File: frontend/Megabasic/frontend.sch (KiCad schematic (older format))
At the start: 27 parts, among them CN1 EDGE, CN2 BREAKOUT, P1 CONN_01X02, P2 CONN_01X02, P3 CONN_01X02, P4 CONN_01X02, P5 CONN_01X02, P6 CONN_01X12, Q1 2N7000, T1 4:1, T2 8:1, U1 4050, U2 74LS145

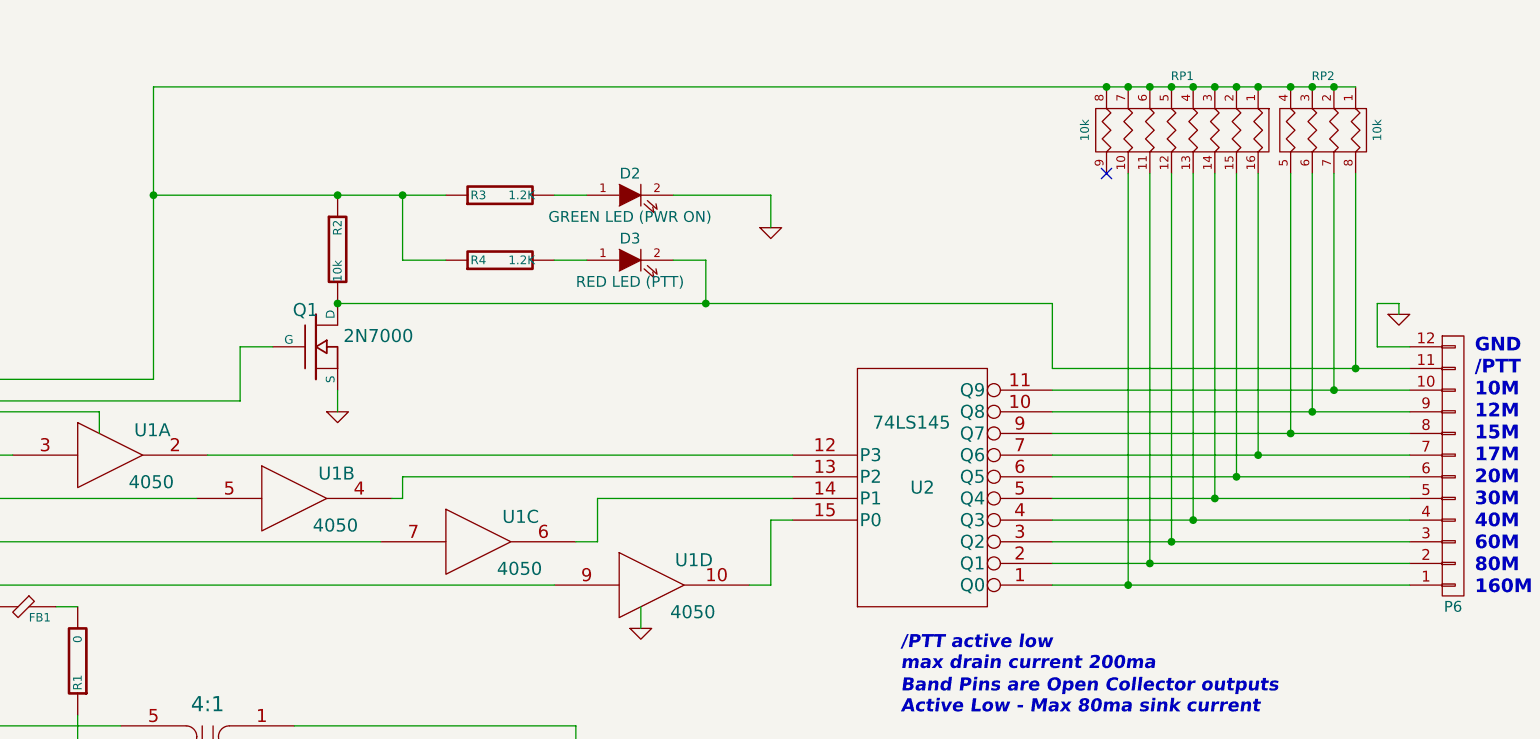
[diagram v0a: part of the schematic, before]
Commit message: modify mounting holes
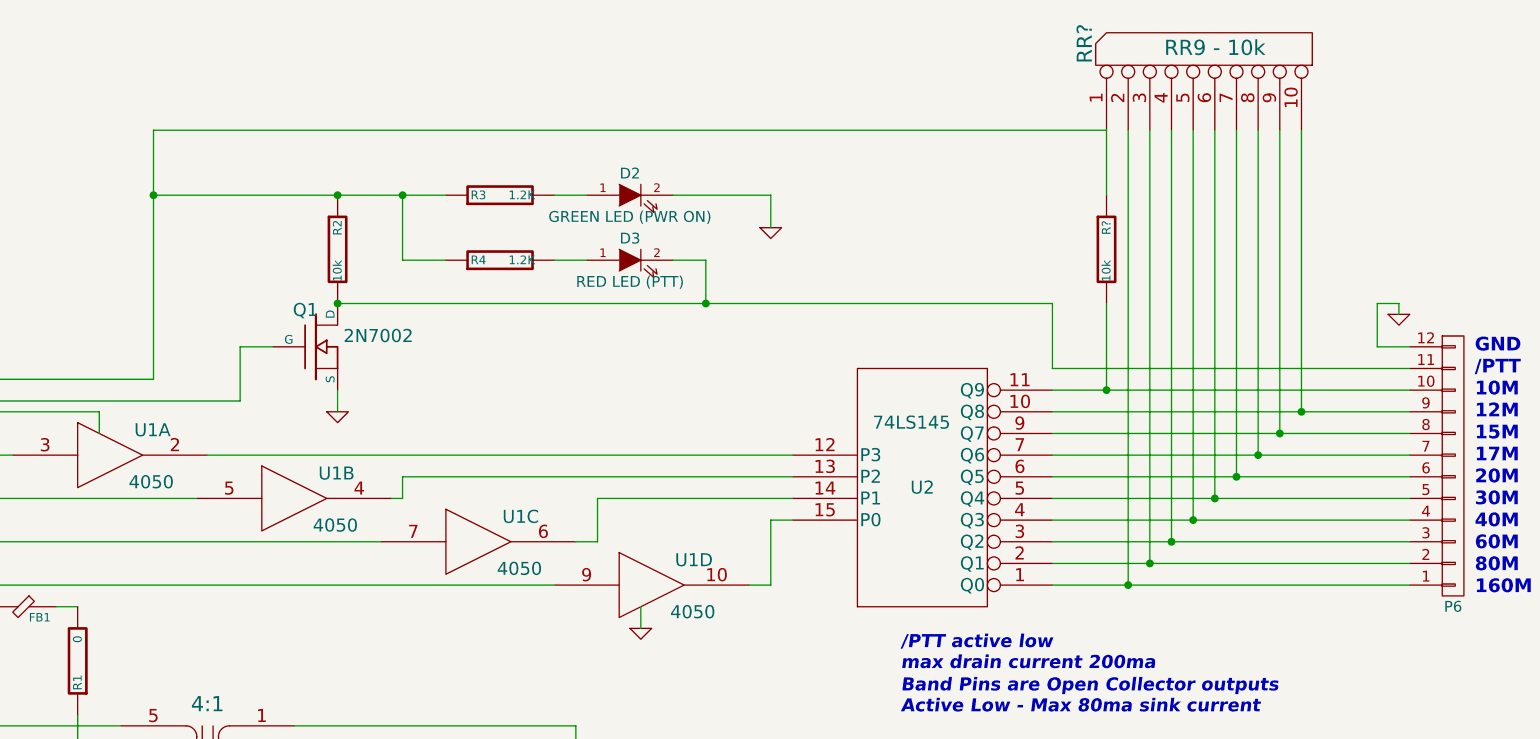
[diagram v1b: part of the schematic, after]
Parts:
- removed RP1: 10k, symbol R_PACK8
- removed RP2: 10k, symbol R_PACK4
- added R?: 10k, symbol R
- added RR?: RR9 - 10k, symbol RR9
- C1, C2, C3, C4, FB1, R1: footprint (none) -> SMD_Packages:SMD-0805
- CN1: footprint (none) -> HERMESLITE:EDGE
- CN2: footprint (none) -> HERMESLITE:BREAKOUT
- D1: footprint (none) -> HERMESLITE:SOD323
- D2, D3: footprint (none) -> LEDs:LED-0805
- P1, P2, P3, P4, P5, P6: footprint (none) -> Pin_Headers:Pin_Header_Straight_1x02
- Q1: value 2N7000 -> 2N7002; footprint (none) -> HERMESLITE:SOT-23-GDS
- R2, R3, R4: footprint (none) -> Resistors_SMD:R_0805_HandSoldering
- T1, T2: footprint (none) -> HERMESLITE:TRANSFREV
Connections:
- net at CN1.A11 (12V), CN1.A12 (12V), CN2.6 (12V)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: now also R?.1, RR?.1 (COM)
- net at P6.1 (P1), U2.1 (Q0): now also RR?.2
- net at P6.10 (P10), U2.11 (Q9): now also R?.2
- net at P6.2 (P2), U2.2 (Q1): now also RR?.3
- net at P6.3 (P3), U2.3 (Q2): now also RR?.4
- net at P6.4 (P4), U2.4 (Q3): now also RR?.5
- net at P6.5 (P5), U2.5 (Q4): now also RR?.6
- net at P6.6 (P6), U2.6 (Q5): now also RR?.7
- net at P6.7 (P7), U2.7 (Q6): now also RR?.8
- net at P6.8 (P8), U2.9 (Q7): now also RR?.9
- net at P6.9 (P9), U2.10 (Q8): now also RR?.10
- no-connect marks 1 -> 0
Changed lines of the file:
@@
 F 0 "CN1" H 1950 3750 60  0000 C CNN
 F 1 "EDGE" H 1950 5800 60  0000 C CNN
-F 2 "" H 1950 4400 60  0000 C CNN
+F 2 "HERMESLITE:EDGE" H 1950 4400 60  0001 C CNN
 F 3 "" H 1950 4400 60  0000 C CNN
 	1    1950 4900
@@
 F 0 "T2" H 4400 5450 70  0000 C CNN
 F 1 "8:1" H 4400 6050 70  0000 C CNN
-F 2 "" H 4400 5750 60  0000 C CNN
+F 2 "HERMESLITE:TRANSFREV" H 4400 5750 60  0001 C CNN
 F 3 "" H 4400 5750 60  0000 C CNN
 	1    4400 5750
@@
 F 0 "T1" H 4400 4000 70  0000 C CNN
 F 1 "4:1" H 4400 4600 70  0000 C CNN
-F 2 "" H 4400 4300 60  0000 C CNN
+F 2 "HERMESLITE:TRANSFREV" H 4400 4300 60  0001 C CNN
 F 3 "" H 4400 4300 60  0000 C CNN
 	1    4400 4300
@@
 F 0 "C3" V 5050 5450 30  0000 L CNN
 F 1 "0.1 uF" V 5050 5600 30  0000 L CNN
-F 2 "" H 5100 5550 60  0000 C CNN
+F 2 "SMD_Packages:SMD-0805" H 5100 5550 60  0001 C CNN
 F 3 "" H 5100 5550 60  0000 C CNN
 	1    5100 5550
@@
 F 0 "C4" V 5450 5450 30  0000 L CNN
 F 1 "0.1 uF" V 5450 5600 30  0000 L CNN
-F 2 "" H 5500 5550 60  0000 C CNN
+F 2 "SMD_Packages:SMD-0805" H 5500 5550 60  0001 C CNN
 F 3 "" H 5500 5550 60  0000 C CNN
 	1    5500 5550
@@
 F 0 "C2" H 3825 6250 30  0000 L CNN
 F 1 "0.1 uF" H 3825 6150 30  0000 L CNN
-F 2 "" H 3800 6200 60  0000 C CNN
+F 2 "SMD_Packages:SMD-0805" H 3800 6200 60  0001 C CNN
 F 3 "" H 3800 6200 60  0000 C CNN
 	1    3800 6200
@@
 F 0 "D1" V 5300 5950 40  0000 C CNN
 F 1 "DIODESCH2" H 5300 5575 40  0001 C CNN
-F 2 "" H 5300 5825 60  0000 C CNN
+F 2 "HERMESLITE:SOD323" H 5300 5825 60  0001 C CNN
 F 3 "" H 5300 5825 60  0000 C CNN
 	1    5300 5750
@@
 F 0 "R1" V 3800 3900 40  0000 C CNN
 F 1 "0" V 3800 3700 40  0000 C CNN
-F 2 "" V 3730 3800 30  0000 C CNN
+F 2 "SMD_Packages:SMD-0805" V 3730 3800 30  0001 C CNN
 F 3 "" H 3800 3800 30  0000 C CNN
 	1    3800 3800
@@
 F 0 "C1" H 3825 4750 30  0000 L CNN
 F 1 "0.1 uF" H 3825 4650 30  0000 L CNN
-F 2 "" H 3800 4700 60  0000 C CNN
+F 2 "SMD_Packages:SMD-0805" H 3800 4700 60  0001 C CNN
 F 3 "" H 3800 4700 60  0000 C CNN
 	1    3800 4700
@@
 F 0 "FB1" H 3625 3500 39  0000 C CNN
 F 1 "FB" H 3550 3650 60  0001 C CNN
-F 2 "" H 3550 3550 60  0000 C CNN
+F 2 "SMD_Packages:SMD-0805" H 3550 3550 60  0001 C CNN
 F 3 "" H 3550 3550 60  0000 C CNN
 	1    3550 3550
@@
 F 0 "CN2" V 2300 800 60  0000 C CNN
 F 1 "BREAKOUT" V 2300 1750 60  0000 C CNN
-F 2 "" H 2250 1300 60  0000 C CNN
+F 2 "HERMESLITE:BREAKOUT" H 2250 1300 60  0001 C CNN
 F 3 "" H 2250 1300 60  0000 C CNN
 	1    2250 1800
@@
 P 4900 2350
 F 0 "Q1" H 4910 2520 60  0000 R CNN
-F 1 "2N7000" H 5350 2400 60  0000 R CNN
-F 2 "" H 4900 2350 60  0000 C CNN
+F 1 "2N7002" H 5350 2400 60  0000 R CNN
+F 2 "HERMESLITE:SOT-23-GDS" H 4900 2350 60  0001 C CNN
 F 3 "" H 4900 2350 60  0000 C CNN
 	1    4900 2350
@@
 F 0 "D2" H 6350 1750 50  0000 C CNN
 F 1 "GREEN LED (PWR ON)" H 6350 1550 50  0000 C CNN
-F 2 "" H 6350 1650 60  0000 C CNN
+F 2 "LEDs:LED-0805" H 6350 1650 60  0001 C CNN
 F 3 "" H 6350 1650 60  0000 C CNN
 	1    6350 1650
@@
 F 0 "R3" V 5750 1750 40  0000 C CNN
 F 1 "1.2K" V 5750 1550 40  0000 C CNN
-F 2 "" V 5680 1650 30  0000 C CNN
+F 2 "Resistors_SMD:R_0805_HandSoldering" V 5680 1650 30  0001 C CNN
 F 3 "" H 5750 1650 30  0000 C CNN
 	1    5750 1650
@@
 F 0 "R4" V 5750 2050 40  0000 C CNN
 F 1 "1.2K" V 5750 1850 40  0000 C CNN
-F 2 "" V 5680 1950 30  0000 C CNN
+F 2 "Resistors_SMD:R_0805_HandSoldering" V 5680 1950 30  0001 C CNN
 F 3 "" H 5750 1950 30  0000 C CNN
 	1    5750 1950
@@
 F 0 "D3" H 6350 2050 50  0000 C CNN
 F 1 "RED LED (PTT)" H 6350 1850 50  0000 C CNN
-F 2 "" H 6350 1950 60  0000 C CNN
+F 2 "LEDs:LED-0805" H 6350 1950 60  0001 C CNN
 F 3 "" H 6350 1950 60  0000 C CNN
 	1    6350 1950
@@
 F 0 "P5" H 9200 5950 50  0000 C CNN
 F 1 "CONN_01X02" V 9300 5800 50  0000 C CNN
-F 2 "" H 9200 5800 60  0000 C CNN
+F 2 "Pin_Headers:Pin_Header_Straight_1x02" H 9200 5800 60  0001 C CNN
 F 3 "" H 9200 5800 60  0000 C CNN
 	1    9200 5800
@@
 F 0 "R2" V 5000 2000 40  0000 C CNN
 F 1 "10k" V 5000 1800 40  0000 C CNN
-F 2 "" V 4930 1900 30  0000 C CNN
+F 2 "Resistors_SMD:R_0805_HandSoldering" V 4930 1900 30  0001 C CNN
 F 3 "" H 5000 1900 30  0000 C CNN
 	1    5000 1900
@@
 F 0 "P4" H 9200 5250 50  0000 C CNN
 F 1 "CONN_01X02" V 9300 5100 50  0000 C CNN
-F 2 "" H 9200 5100 60  0000 C CNN
+F 2 "Pin_Headers:Pin_Header_Straight_1x02" H 9200 5100 60  0001 C CNN
 F 3 "" H 9200 5100 60  0000 C CNN
 	1    9200 5100
@@
 F 0 "P6" H 10150 3550 50  0000 C CNN
 F 1 "CONN_01X12" V 10250 2900 50  0001 C CNN
-F 2 "" H 10150 2900 60  0000 C CNN
+F 2 "Pin_Headers:Pin_Header_Straight_1x02" H 10150 2900 60  0001 C CNN
 F 3 "" H 10150 2900 60  0000 C CNN
 	1    10150 2900
@@
 Wire Wire Line
 	4150 2500 2150 2500
-Wire Wire Line
-	4150 1150 4150 2500
 Connection ~ 2150 2500
 Connection ~ 3250 2600
@@
 F 0 "U2" H 7700 3000 60  0000 C CNN
 F 1 "74LS145" H 7650 2700 60  0000 C CNN
-F 2 "" H 7700 3000 60  0000 C CNN
+F 2 "" H 7700 3000 60  0001 C CNN
 F 3 "" H 7700 3000 60  0000 C CNN
 	1    7700 3000
@@
 F 0 "U1" H 4145 2965 60  0000 C CNN
 F 1 "4050" H 4140 2725 60  0000 C CNN
-F 2 "" H 3950 2850 60  0000 C CNN
+F 2 "" H 3950 2850 60  0001 C CNN
 F 3 "" H 3950 2850 60  0000 C CNN
 	1    3950 2850
@@
 F 0 "U1" H 4995 3165 60  0000 C CNN
 F 1 "4050" H 4990 2925 60  0000 C CNN
-F 2 "" H 4800 3050 60  0000 C CNN
+F 2 "" H 4800 3050 60  0001 C CNN
 F 3 "" H 4800 3050 60  0000 C CNN
 	2    4800 3050
@@
 F 0 "U1" H 5845 3365 60  0000 C CNN
 F 1 "4050" H 5840 3125 60  0000 C CNN
-F 2 "" H 5650 3250 60  0000 C CNN
+F 2 "" H 5650 3250 60  0001 C CNN
 F 3 "" H 5650 3250 60  0000 C CNN
 	3    5650 3250
@@
 F 0 "U1" H 6645 3565 60  0000 C CNN
 F 1 "4050" H 6640 3325 60  0000 C CNN
-F 2 "" H 6450 3450 60  0000 C CNN
+F 2 "" H 6450 3450 60  0001 C CNN
 F 3 "" H 6450 3450 60  0000 C CNN
 	4    6450 3450
@@
 F 0 "P3" H 3100 5300 50  0000 C CNN
 F 1 "CONN_01X02" V 3200 5150 50  0000 C CNN
-F 2 "" H 3100 5150 60  0000 C CNN
+F 2 "Pin_Headers:Pin_Header_Straight_1x02" H 3100 5150 60  0001 C CNN
 F 3 "" H 3100 5150 60  0000 C CNN
 	1    3100 5150
@@
 F 0 "P1" H 700 5300 50  0000 C CNN
 F 1 "CONN_01X02" V 800 5150 50  0000 C CNN
-F 2 "" H 700 5150 60  0000 C CNN
+F 2 "Pin_Headers:Pin_Header_Straight_1x02" H 700 5150 60  0001 C CNN
 F 3 "" H 700 5150 60  0000 C CNN
 	1    700  5150
@@
 F 0 "P2" H 700 5700 50  0000 C CNN
 F 1 "CONN_01X02" V 800 5550 50  0000 C CNN
-F 2 "" H 700 5550 60  0000 C CNN
+F 2 "Pin_Headers:Pin_Header_Straight_1x02" H 700 5550 60  0001 C CNN
 F 3 "" H 700 5550 60  0000 C CNN
 	1    700  5550
@@
 Wire Wire Line
 	950  5600 950  5700
-$Comp
-L R_PACK8 RP1
-U 1 1 54DFB23D
-P 8900 1350
-F 0 "RP1" V 8650 1350 40  0000 C CNN
-F 1 "10k" H 8900 900 40  0000 C CNN
-F 2 "" H 8900 1350 60  0000 C CNN
-F 3 "" H 8900 1350 60  0000 C CNN
-	1    8900 1350
-	0    1    1    0
-$EndComp
-$Comp
-L R_PACK4 RP2
-U 1 1 54DFB264
-P 9350 1350
-F 0 "RP2" V 9100 1550 40  0000 C CNN
-F 1 "10k" H 9350 1800 40  0000 C CNN
-F 2 "" H 9350 1350 60  0000 C CNN
-F 3 "" H 9350 1350 60  0000 C CNN
-	1    9350 1350
-	0    1    1    0
-$EndComp
 Wire Wire Line
 	6000 5150 9000 5150
@@
 	6100 4100 4800 4100
 Wire Wire Line
-	9700 1550 9700 2450
-Connection ~ 9700 2450
-Wire Wire Line
-	9600 1550 9600 2550
-Connection ~ 9600 2550
-Wire Wire Line
-	9500 1550 9500 2650
-Connection ~ 9500 2650
-Wire Wire Line
-	9400 1550 9400 2750
-Connection ~ 9400 2750
-Wire Wire Line
-	9250 1550 9250 2850
+	9250 1350 9250 2850
 Connection ~ 9250 2850
 Wire Wire Line
-	9150 1550 9150 2950
+	9150 1350 9150 2950
 Connection ~ 9150 2950
 Wire Wire Line
-	9050 1550 9050 3050
+	9050 1350 9050 3050
 Connection ~ 9050 3050
 Wire Wire Line
-	8950 1550 8950 3150
+	8950 1350 8950 3150
 Connection ~ 8950 3150
 Wire Wire Line
-	8850 1550 8850 3250
+	8850 1350 8850 3250
 Connection ~ 8850 3250
 Wire Wire Line
-	8750 1550 8750 3350
+	8750 1350 8750 3350
 Connection ~ 8750 3350
 Wire Wire Line
-	8650 1550 8650 3450
+	8650 1350 8650 3450
 Connection ~ 8650 3450
-Wire Wire Line
-	4150 1150 9700 1150
-Connection ~ 8650 1150
-Connection ~ 8750 1150
-Connection ~ 8850 1150
-Connection ~ 8950 1150
-Connection ~ 9050 1150
-Connection ~ 9150 1150
-Connection ~ 9250 1150
-Connection ~ 9400 1150
-Connection ~ 9500 1150
-Connection ~ 9600 1150
-Connection ~ 8550 1150
 Connection ~ 4150 1650
 Wire Wire Line
@@
 	1    0    0    -1
 $EndComp
-NoConn ~ 8550 1550
+$Comp
+L RR9 RR?
+U 1 1 54F13952
+P 9050 1000
+F 0 "RR?" H 9100 1600 70  0000 C CNN
+F 1 "RR9 - 10k" V 9080 1000 70  0000 C CNN
+F 2 "" H 9050 1000 60  0000 C CNN
+F 3 "" H 9050 1000 60  0000 C CNN
+	1    9050 1000
+	0    -1   -1   0
+$EndComp
+Wire Wire Line
+	9350 2750 9350 1350
+Connection ~ 9350 2750
+Wire Wire Line
+	9450 1350 9450 2650
+Connection ~ 9450 2650
+Wire Wire Line
+	8550 1350 4150 1350
+Wire Wire Line
+	4150 1350 4150 2500
+$Comp
+L R R?
+U 1 1 54F169D2
+P 8550 1900
+F 0 "R?" V 8550 2000 40  0000 C CNN
+F 1 "10k" V 8550 1800 40  0000 C CNN
+F 2 "" V 8480 1900 30  0001 C CNN
+F 3 "" H 8550 1900 30  0000 C CNN
+	1    8550 1900
+	1    0    0    -1
+$EndComp
+Wire Wire Line
+	8550 1350 8550 1650
+Wire Wire Line
+	8550 2150 8550 2550
+Connection ~ 8550 2550
 $EndSCHEMATC

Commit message: final 1.2 changes
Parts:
- removed P1, P2, P3, P4, P5: CONN_01X02, Pin_Headers:Pin_Header_Straight_1x02, symbol CONN_01X02
- added J1, J2: SMA, HERMESLITE:SMA, symbol SMA
- R1: footprint SMD_Packages:SMD-0805 -> Resistors_SMD:R_0805_HandSoldering
- R5: renamed from R?; footprint (none) -> Resistors_SMD:R_0805_HandSoldering
- RR1: renamed from RR?; footprint (none) -> Discret:r_pack9
- U1, U2: footprint (none) -> Housings_SOIC:SOIC-16_3.9x9.9mm_Pitch1.27mm
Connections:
- net at D1.2 (K), T2.2 (S2): now also J2.2 (GND1), J2.3 (GND2), J2.4 (GND3), J2.5 (GND4)
- net at T1.1 (S1): now also J1.1 (RF)
- net at T1.2 (S2): now also J1.2 (GND1), J1.3 (GND2), J1.4 (GND3), J1.5 (GND4)
- net at C4.1: now also J2.1 (RF)
- no-connect marks 0 -> 2
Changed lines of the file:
@@
 F 0 "R1" V 3800 3900 40  0000 C CNN
 F 1 "0" V 3800 3700 40  0000 C CNN
-F 2 "SMD_Packages:SMD-0805" V 3730 3800 30  0001 C CNN
+F 2 "Resistors_SMD:R_0805_HandSoldering" V 3730 3800 30  0001 C CNN
 F 3 "" H 3800 3800 30  0000 C CNN
 	1    3800 3800
@@
 Wire Wire Line
 	1200 5000 1200 6100
-Wire Wire Line
-	900  5100 1350 5100
 Connection ~ 1200 5100
 Wire Wire Line
 	1350 5200 1200 5200
 Connection ~ 1200 5200
-Wire Wire Line
-	950  5300 1350 5300
 Connection ~ 1200 5300
 Wire Wire Line
 	1350 5400 1200 5400
 Connection ~ 1200 5400
-Wire Wire Line
-	900  5500 1350 5500
 Connection ~ 1200 5500
 Wire Wire Line
 	1350 5600 1200 5600
 Connection ~ 1200 5600
-Wire Wire Line
-	950  5700 1350 5700
 Connection ~ 1200 5700
 Wire Wire Line
@@
 	3650 5950 4000 5950
 Wire Wire Line
-	2550 5200 2900 5200
-Wire Wire Line
-	2550 5100 2900 5100
-Wire Wire Line
-	4800 5950 7900 5950
+	4800 5950 9200 5950
 $Comp
 L MOSFET_N Q1
@@
 	6550 1950 6700 1950
 $Comp
-L CONN_01X02 P5
-U 1 1 54DE891D
-P 9200 5800
-F 0 "P5" H 9200 5950 50  0000 C CNN
-F 1 "CONN_01X02" V 9300 5800 50  0000 C CNN
-F 2 "Pin_Headers:Pin_Header_Straight_1x02" H 9200 5800 60  0001 C CNN
-F 3 "" H 9200 5800 60  0000 C CNN
-	1    9200 5800
-	1    0    0    -1
-$EndComp
-$Comp
 L R R2
 U 1 1 54DE8DE6
@@
 F 3 "" H 5000 1900 30  0000 C CNN
 	1    5000 1900
-	1    0    0    -1
-$EndComp
-$Comp
-L CONN_01X02 P4
-U 1 1 54DF6135
-P 9200 5100
-F 0 "P4" H 9200 5250 50  0000 C CNN
-F 1 "CONN_01X02" V 9300 5100 50  0000 C CNN
-F 2 "Pin_Headers:Pin_Header_Straight_1x02" H 9200 5100 60  0001 C CNN
-F 3 "" H 9200 5100 60  0000 C CNN
-	1    9200 5100
 	1    0    0    -1
 $EndComp
@@
 F 0 "U2" H 7700 3000 60  0000 C CNN
 F 1 "74LS145" H 7650 2700 60  0000 C CNN
-F 2 "" H 7700 3000 60  0001 C CNN
+F 2 "Housings_SOIC:SOIC-16_3.9x9.9mm_Pitch1.27mm" H 7700 3000 60  0001 C CNN
 F 3 "" H 7700 3000 60  0000 C CNN
 	1    7700 3000
@@
 F 0 "U1" H 4145 2965 60  0000 C CNN
 F 1 "4050" H 4140 2725 60  0000 C CNN
-F 2 "" H 3950 2850 60  0001 C CNN
+F 2 "Housings_SOIC:SOIC-16_3.9x9.9mm_Pitch1.27mm" H 3950 2850 60  0001 C CNN
 F 3 "" H 3950 2850 60  0000 C CNN
 	1    3950 2850
@@
 F 0 "U1" H 4995 3165 60  0000 C CNN
 F 1 "4050" H 4990 2925 60  0000 C CNN
-F 2 "" H 4800 3050 60  0001 C CNN
+F 2 "Housings_SOIC:SOIC-16_3.9x9.9mm_Pitch1.27mm" H 4800 3050 60  0001 C CNN
 F 3 "" H 4800 3050 60  0000 C CNN
 	2    4800 3050
@@
 F 0 "U1" H 5845 3365 60  0000 C CNN
 F 1 "4050" H 5840 3125 60  0000 C CNN
-F 2 "" H 5650 3250 60  0001 C CNN
+F 2 "Housings_SOIC:SOIC-16_3.9x9.9mm_Pitch1.27mm" H 5650 3250 60  0001 C CNN
 F 3 "" H 5650 3250 60  0000 C CNN
 	3    5650 3250
@@
 F 0 "U1" H 6645 3565 60  0000 C CNN
 F 1 "4050" H 6640 3325 60  0000 C CNN
-F 2 "" H 6450 3450 60  0001 C CNN
+F 2 "Housings_SOIC:SOIC-16_3.9x9.9mm_Pitch1.27mm" H 6450 3450 60  0001 C CNN
 F 3 "" H 6450 3450 60  0000 C CNN
 	4    6450 3450
@@
 /PTT active low\nmax drain current 200ma
 Wire Wire Line
-	7900 5950 7900 5850
-Wire Wire Line
-	7900 5850 9000 5850
-Wire Wire Line
 	7900 5550 7900 5750
 Wire Wire Line
 	7900 5750 9000 5750
-$Comp
-L CONN_01X02 P3
-U 1 1 54DFA723
-P 3100 5150
-F 0 "P3" H 3100 5300 50  0000 C CNN
-F 1 "CONN_01X02" V 3200 5150 50  0000 C CNN
-F 2 "Pin_Headers:Pin_Header_Straight_1x02" H 3100 5150 60  0001 C CNN
-F 3 "" H 3100 5150 60  0000 C CNN
-	1    3100 5150
-	1    0    0    -1
-$EndComp
-$Comp
-L CONN_01X02 P1
-U 1 1 54DFA9CA
-P 700 5150
-F 0 "P1" H 700 5300 50  0000 C CNN
-F 1 "CONN_01X02" V 800 5150 50  0000 C CNN
-F 2 "Pin_Headers:Pin_Header_Straight_1x02" H 700 5150 60  0001 C CNN
-F 3 "" H 700 5150 60  0000 C CNN
-	1    700  5150
-	-1   0    0    1
-$EndComp
-$Comp
-L CONN_01X02 P2
-U 1 1 54DFAA50
-P 700 5550
-F 0 "P2" H 700 5700 50  0000 C CNN
-F 1 "CONN_01X02" V 800 5550 50  0000 C CNN
-F 2 "Pin_Headers:Pin_Header_Straight_1x02" H 700 5550 60  0001 C CNN
-F 3 "" H 700 5550 60  0000 C CNN
-	1    700  5550
-	-1   0    0    1
-$EndComp
-Wire Wire Line
-	900  5200 950  5200
-Wire Wire Line
-	950  5200 950  5300
-Wire Wire Line
-	900  5600 950  5600
-Wire Wire Line
-	950  5600 950  5700
-Wire Wire Line
-	6000 5150 9000 5150
 Wire Wire Line
 	6100 5050 9000 5050
 Wire Wire Line
-	6000 5150 6000 4500
+	6000 4500 6000 5250
 Wire Wire Line
 	6000 4500 4800 4500
@@
 $EndComp
 $Comp
-L RR9 RR?
+L RR9 RR1
 U 1 1 54F13952
 P 9050 1000
-F 0 "RR?" H 9100 1600 70  0000 C CNN
+F 0 "RR1" H 9100 1600 70  0000 C CNN
 F 1 "RR9 - 10k" V 9080 1000 70  0000 C CNN
-F 2 "" H 9050 1000 60  0000 C CNN
+F 2 "Discret:r_pack9" H 9050 1000 60  0001 C CNN
 F 3 "" H 9050 1000 60  0000 C CNN
 	1    9050 1000
@@
 	4150 1350 4150 2500
 $Comp
-L R R?
+L R R5
 U 1 1 54F169D2
 P 8550 1900
-F 0 "R?" V 8550 2000 40  0000 C CNN
+F 0 "R5" V 8550 2000 40  0000 C CNN
 F 1 "10k" V 8550 1800 40  0000 C CNN
-F 2 "" V 8480 1900 30  0001 C CNN
+F 2 "Resistors_SMD:R_0805_HandSoldering" V 8480 1900 30  0001 C CNN
 F 3 "" H 8550 1900 30  0000 C CNN
 	1    8550 1900
@@
 	8550 2150 8550 2550
 Connection ~ 8550 2550
+$Comp
+L SMA J1
+U 1 1 550A2257
+P 9150 5350
+F 0 "J1" H 9275 5665 60  0000 C CNN
+F 1 "SMA" H 9340 5590 60  0000 C CNN
+F 2 "HERMESLITE:SMA" H 9325 5520 50  0000 C CNN
+F 3 "" H 9150 5350 60  0000 C CNN
+	1    9150 5350
+	1    0    0    -1
+$EndComp
+$Comp
+L SMA J2
+U 1 1 550A240A
+P 9150 6050
+F 0 "J2" H 9275 6365 60  0000 C CNN
+F 1 "SMA" H 9340 6290 60  0000 C CNN
+F 2 "HERMESLITE:SMA" H 9325 6220 50  0000 C CNN
+F 3 "" H 9150 6050 60  0000 C CNN
+	1    9150 6050
+	1    0    0    -1
+$EndComp
+Connection ~ 9050 5950
+Connection ~ 9100 5950
+Connection ~ 9150 5950
+Wire Wire Line
+	6000 5250 9200 5250
+Connection ~ 9150 5250
+Connection ~ 9100 5250
+Connection ~ 9050 5250
+Wire Wire Line
+	1200 5100 1350 5100
+Wire Wire Line
+	1200 5300 1350 5300
+Wire Wire Line
+	1200 5700 1350 5700
+Wire Wire Line
+	1200 5500 1350 5500
+NoConn ~ 2550 5100
+NoConn ~ 2550 5200
+Connection ~ 9200 5950
+Connection ~ 9200 5250
 $EndSCHEMATC
